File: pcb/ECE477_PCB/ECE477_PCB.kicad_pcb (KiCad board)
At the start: 2 copper layers, 96.2 x 40.6 mm, 95 parts, among them J1 DEBUG, J10 ToF 5, J2 USB_B_Micro, J3 ESC, J4 ELRS, J5 AUX_PWR, J6 ToF 1, J7 ToF 2, J8 ToF 3, J9 ToF 4, M1 Brushed_DC, M2 Brushed_DC, M3 Brushed_DC, M4 Brushed_DC, Q1 IRLML6244TR, Q2 IRLML6244TR, Q3 IRLML6244TR, Q4 IRLML6244TR, SW1 RESET, U1 STM32F446RETx, U2 Pololu_S13V10F5, U3 REG1117-3.3, U4 FT230XQ, U5 MPU-9250, U6 LSM6DS3, Y1 16MHz X322516MLB4SI

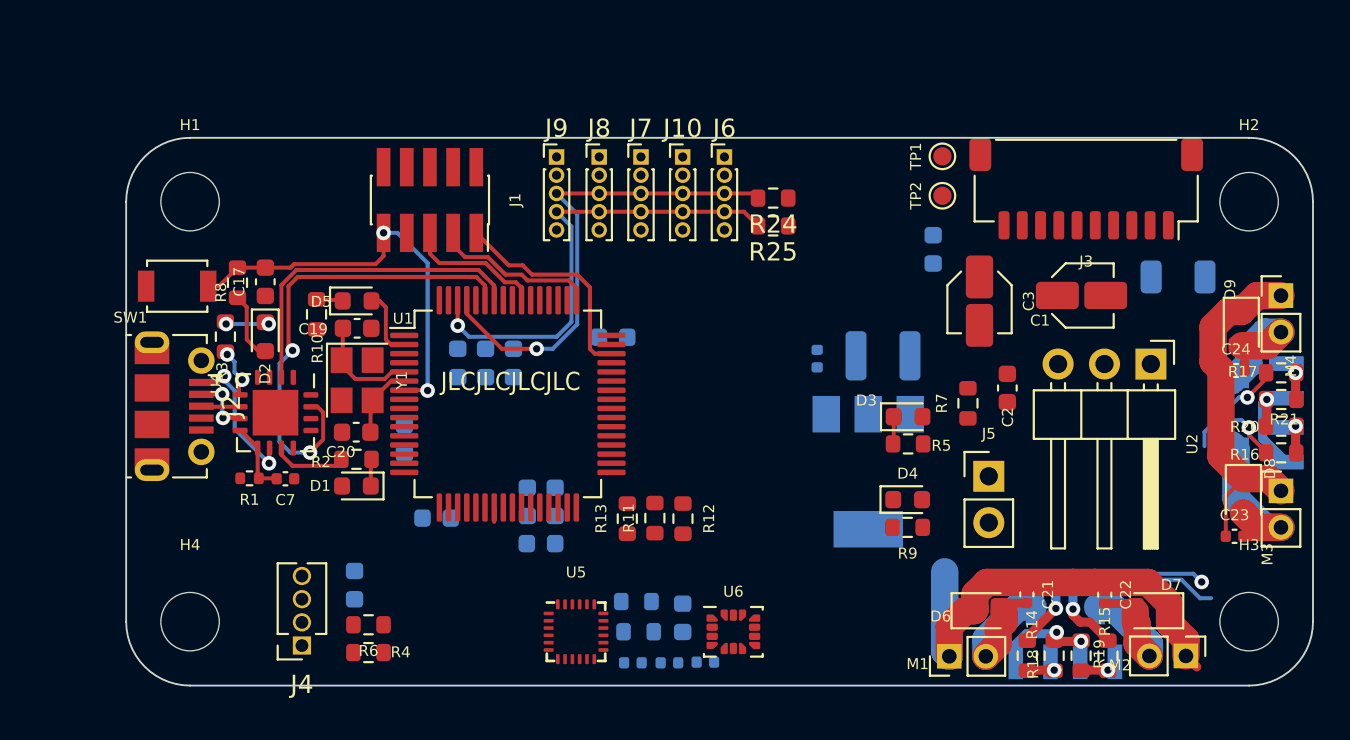
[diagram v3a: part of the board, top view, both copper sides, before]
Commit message: getting pretty close. fixed DRC errors, moved UARTS and radio connector, added pi zero connector
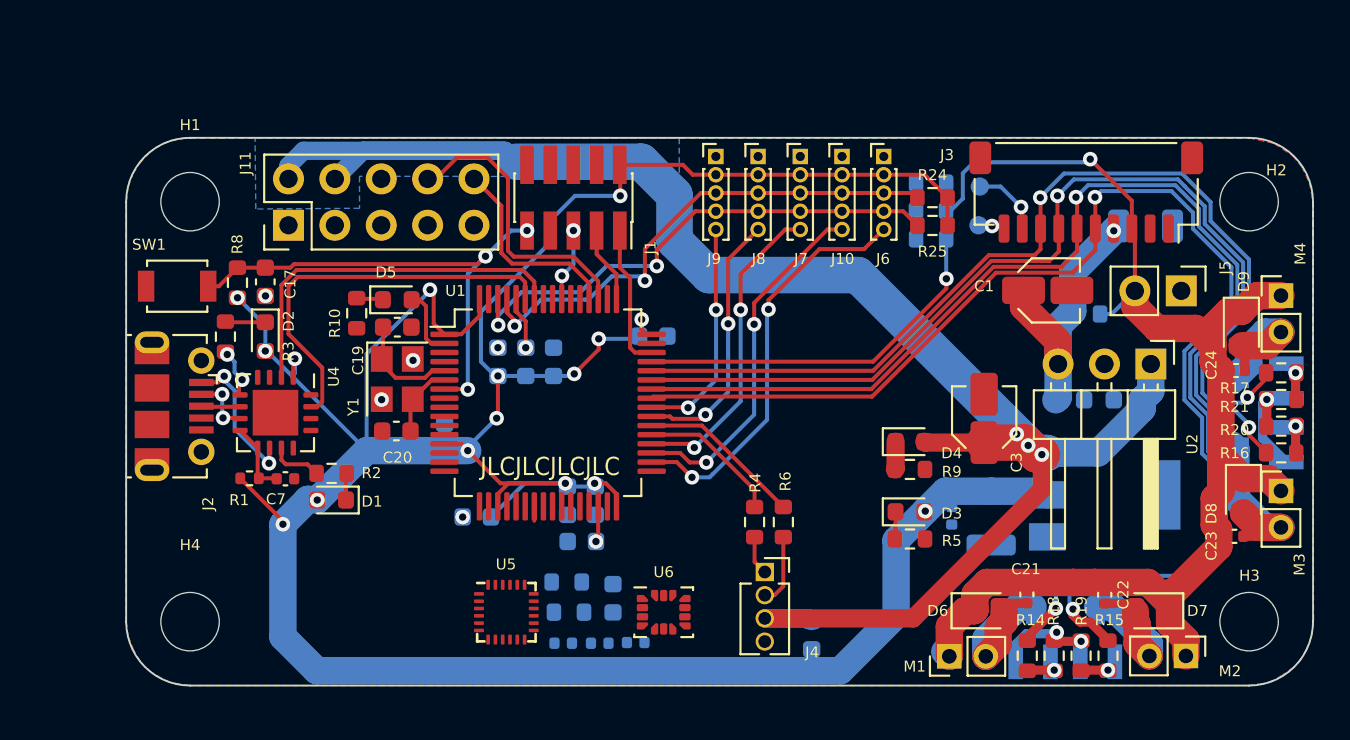
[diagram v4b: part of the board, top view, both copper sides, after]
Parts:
- added J11: Pi Zero, Connector_PinHeader_2.54mm:PinHeader_2x05_P2.54mm_Vertical, F.Cu at (56.8, 32.8)
- C2, R12, R13, R7, TP1, TP2: moved to B.Cu
- R11: value 30K -> 10K; moved to B.Cu
- moved J4 25.7 mm to (82.9, 51.7), turned to 0 degrees
- moved C16 25.2 mm to (85.4, 55.2), turned to 90 degrees
- moved R13 24.8 mm to (92.0, 30.4), turned to 0 degrees
- moved R6 23.4 mm to (83.9, 49.0), turned to -90 degrees
- moved R11 22.6 mm to (92.0, 32.0), turned to 180 degrees
- moved R4 22.3 mm to (82.3, 49.0), turned to 90 degrees
- moved R12 20.5 mm to (92.0, 33.5), turned to 0 degrees
- moved J5 14.6 mm to (105.7, 36.3), turned to -90 degrees
- moved C4 13.5 mm to (102.8, 42.3), turned to 180 degrees
- moved U3 13.0 mm to (101.5, 47.5), turned to 0 degrees
- moved C6 11.3 mm to (93.1, 48.7)
- moved C5 10.7 mm to (95.3, 48.8), turned to -90 degrees
- moved J10 8.73 mm to (87.1, 29.0)
- moved J7 8.73 mm to (84.8, 29.0)
- moved J6 8.73 mm to (89.4, 29.0)
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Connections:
- J10 pad 2: +3.3V -> +3V3
- J3 pad MP: (no net) -> GND
- J6 pad 2: +3.3V -> +3V3
- J7 pad 2: +3.3V -> +3V3
- J8 pad 2: +3.3V -> +3V3
- J9 pad 2: +3.3V -> +3V3
- R12 pad 2: unconnected-(R12-Pad2) -> VSENSE
- U1 pad 16: ELRS_RX -> USART2_TX
- U1 pad 17: ELRS_TX -> USART2_RX
- U1 pad 34: unconnected-(U1-Pad34) -> TOF_1_SHTDN
- U1 pad 35: unconnected-(U1-Pad35) -> TOF_5_SHTDN
- U1 pad 36: unconnected-(U1-Pad36) -> TOF_2_SHTDN
- U1 pad 37: unconnected-(U1-Pad37) -> ELRS_RX
- U1 pad 38: unconnected-(U1-Pad38) -> ELRS_TX
- U1 pad 39: unconnected-(U1-Pad39) -> TOF_3_SHTDN
- U1 pad 40: unconnected-(U1-Pad40) -> TOF_4_SHTDN
- U1 pad 41: MOTOR_B -> MOTOR_A
- U1 pad 42: MOTOR_A -> MOTOR_B
- U1 pad 43: MOTOR_D -> MOTOR_C
- U1 pad 44: MOTOR_C -> MOTOR_D
- U1 pad 45: unconnected-(U1-Pad45) -> VSENSE
- U1 pad 51: UART4_RX -> UART4_TX
- U1 pad 52: UART4_TX -> UART4_RX
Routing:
- net +3V3: track 3.77 -> 175.3 mm, vias 0 -> 16
- net +5V: track 0.00 -> 98.3 mm, vias 0 -> 3
- net MOTOR_B: track 12.2 -> 70.8 mm, vias 1 -> 2
- net MOTOR_A: track 12.0 -> 69.9 mm
- net MOTOR_C: track 5.23 -> 55.1 mm, vias 1 -> 2
- net MOTOR_D: track 5.70 -> 54.4 mm, vias 1 -> 2
- net +BATT: track 45.0 -> 76.2 mm, vias 0 -> 1
- net TOF_1_SHTDN: track 0.00 -> 22.5 mm, vias 0 -> 2
- net VSENSE: track 0.00 -> 20.5 mm, vias 0 -> 1
- net TOF_5_SHTDN: track 0.00 -> 19.5 mm, vias 0 -> 2
- net TOF_2_SHTDN: track 0.00 -> 17.3 mm, vias 0 -> 2
- net UART4_TX: track 0.00 -> 16.0 mm
- net +10V: track 0.00 -> 15.8 mm, vias 0 -> 1
- net TOF_3_SHTDN: track 0.00 -> 14.4 mm, vias 0 -> 2
- net TOF_4_SHTDN: track 0.00 -> 12.4 mm, vias 0 -> 2
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- added copper zone on B.Cu, net +5V
- added copper zone on B.Cu, net GND
- added copper zone on F.Cu, net GND
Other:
- board text added: "DNP"

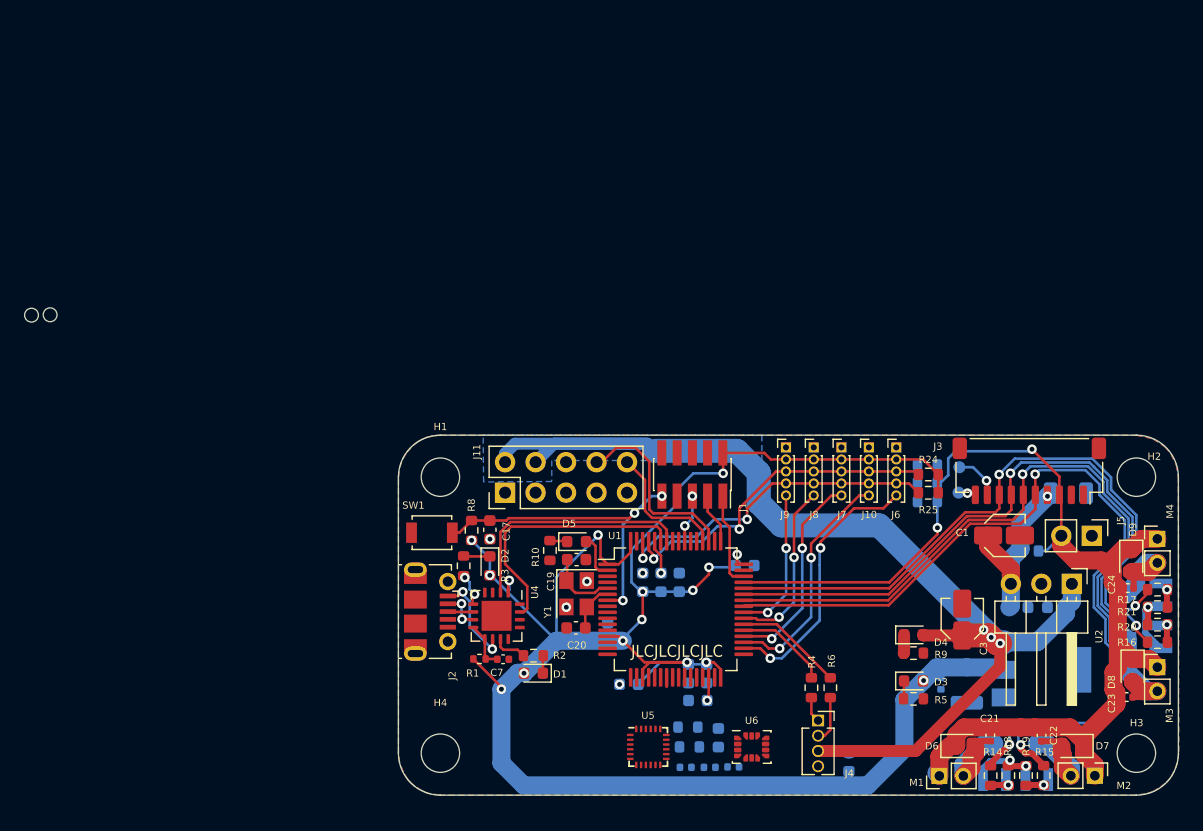
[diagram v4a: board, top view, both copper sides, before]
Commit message: completed first rev of PCB. looks like the Pi connector needs moved slightly, board radius is off but drill positions are still the same
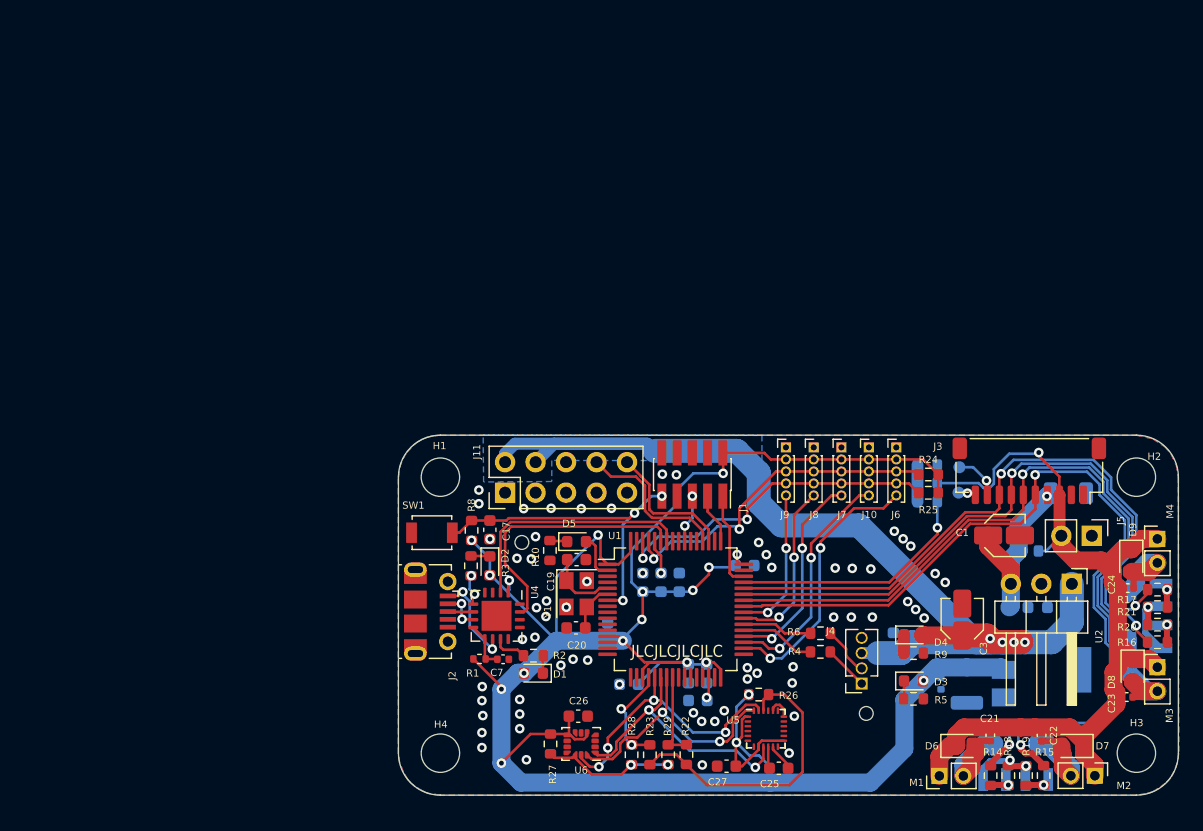
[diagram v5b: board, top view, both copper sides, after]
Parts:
- removed C28: 2.2nF, 50V, Capacitor_SMD:C_0603_1608Metric
- added R26: 4.7k, Resistor_SMD:R_0603_1608Metric, F.Cu at (77.9, 49.6)
- added R27: 4.7k, Resistor_SMD:R_0603_1608Metric, F.Cu at (60.6, 53.7)
- added R28: 0, Resistor_SMD:R_0603_1608Metric, F.Cu at (67.3, 54.6)
- added R29: 0, Resistor_SMD:R_0603_1608Metric, F.Cu at (70.4, 54.6)
- C25: value 10nF, 4V -> 0.1uF 4V; footprint Capacitor_SMD:C_0402_1005Metric -> Capacitor_SMD:C_0603_1608Metric; moved to F.Cu
- C26: footprint Capacitor_SMD:C_0402_1005Metric -> Capacitor_SMD:C_0603_1608Metric; moved to F.Cu
- C27: value 0.1uF 2V -> 0.1uF 4V; footprint Capacitor_SMD:C_0402_1005Metric -> Capacitor_SMD:C_0603_1608Metric; moved to F.Cu
- R22, R23: value 4.7K -> 0; moved to F.Cu
- moved U6 14.2 mm to (63.1, 53.7), turned to 180 degrees
- moved C26 11.8 mm to (62.9, 51.4)
- moved C16 10.7 mm to (89.2, 45.2), turned to -90 degrees
- moved U5 9.91 mm to (78.5, 52.4)
- moved J4 4.76 mm to (86.5, 48.7), turned to 180 degrees
- moved R6 4.61 mm to (83.1, 44.5), turned to 0 degrees
- moved R23 3.92 mm to (68.9, 54.6), turned to -90 degrees
- moved C25 3.79 mm to (79.6, 55.7), turned to 0 degrees
- moved C27 3.41 mm to (75.2, 55.5), turned to 0 degrees
- moved R4 3.08 mm to (83.1, 46.0), turned to 180 degrees
- moved R22 0.69 mm to (71.9, 54.6), turned to -90 degrees
- moved R3 0.61 mm to (53.9, 38.9)
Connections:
- C25 pad 1: GND -> Net-(U5-Pad10)
- C25 pad 2: +3V3 -> GND
- C26 pad 1: +3V3 -> GND
- C26 pad 2: GND -> +3V3
- C27 pad 1: unconnected-(C27-Pad1) -> GND
- C27 pad 2: GND -> +3V3
- R22 pad 1: +3V3 -> SPI1_CS2
- R22 pad 2: unconnected-(R22-Pad2) -> Net-(U5-Pad22)
- R23 pad 1: +3V3 -> SPI1_CS
- R23 pad 2: unconnected-(R23-Pad2) -> Net-(U5-Pad22)
- U1 pad 20: unconnected-(U1-Pad20) -> SPI1_CS
- U1 pad 24: unconnected-(U1-Pad24) -> SPI1_CS2
- U5 pad 1: unconnected-(U5-Pad1) -> +3V3
- U5 pad 10: unconnected-(U5-Pad10) -> Net-(U5-Pad10)
- U5 pad 11: unconnected-(U5-Pad11) -> GND
- U5 pad 13: unconnected-(U5-Pad13) -> +3V3
- U5 pad 18: unconnected-(U5-Pad18) -> GND
- U5 pad 20: unconnected-(U5-Pad20) -> GND
- U5 pad 22: unconnected-(U5-Pad22) -> Net-(U5-Pad22)
- U5 pad 23: unconnected-(U5-Pad23) -> SPI1_SCK
- U5 pad 24: unconnected-(U5-Pad24) -> SPI1_MOSI
- U5 pad 8: unconnected-(U5-Pad8) -> +3V3
- U5 pad 9: unconnected-(U5-Pad9) -> SPI1_MISO
- U6 pad 1: unconnected-(U6-Pad1) -> SPI1_MISO
- U6 pad 12: unconnected-(U6-Pad12) -> Net-(U6-Pad12)
- U6 pad 13: unconnected-(U6-Pad13) -> SPI1_SCK
- U6 pad 14: unconnected-(U6-Pad14) -> SPI1_MOSI
- U6 pad 5: unconnected-(U6-Pad5) -> +3V3
- U6 pad 6: unconnected-(U6-Pad6) -> GND
- U6 pad 7: unconnected-(U6-Pad7) -> GND
- U6 pad 8: unconnected-(U6-Pad8) -> +3V3
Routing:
- net +3V3: track 175.3 -> 205.0 mm, vias 16 -> 19
- net Net-(U5-Pad22): track 0.00 -> 24.5 mm
- net SPI1_SCK: track 0.00 -> 23.3 mm, vias 0 -> 4
- net SPI1_MISO: track 0.00 -> 22.8 mm, vias 0 -> 2
- net SPI1_MOSI: track 0.76 -> 21.7 mm, vias 0 -> 2
- net Net-(U6-Pad12): track 0.00 -> 11.2 mm, vias 0 -> 2
- net SPI1_CS: track 0.00 -> 8.65 mm, vias 0 -> 2
- net SPI1_CS2: track 0.00 -> 7.31 mm
- net UART4_TX: track 16.0 -> 11.3 mm
- net GND: track 16.1 -> 20.5 mm, vias 9 -> 66
- net ELRS_TX: track 9.06 -> 5.89 mm
- net Net-(R11-Pad2): track 0.00 -> 3.06 mm
- net +5V: track 98.3 -> 101.2 mm, vias 3 -> 4
- net UART4_RX: track 11.1 -> 13.3 mm
- net Net-(U5-Pad10): track 0.00 -> 1.85 mm
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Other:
- board size 96.2 x 40.6 mm -> 65 x 30 mm
